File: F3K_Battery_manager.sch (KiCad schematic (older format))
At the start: 12 parts, among them J5 Debug, J6 Serial, J7 Receiver, Q1 CSD13385F5, Q2 CSD13385F5, U1 DRV5032

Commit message: added antenna into schematic
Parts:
- added AE?: Antenna_Loop, symbol Antenna_Loop
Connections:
- no-connect marks 0 -> 2
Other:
- note added: "Antenna - only for Kicost\n"
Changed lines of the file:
@@
 Wire Wire Line
 	2000 4600 2100 4600
+$Comp
+L Antenna_Loop AE?
+U 1 1 5AB2F1C7
+P 1150 4150
+F 0 "AE?" H 1200 4400 50  0000 C CNN
+F 1 "Antenna_Loop" H 1200 4350 50  0000 C CNN
+F 2 "" H 1150 4150 50  0001 C CNN
+F 3 "https://www.vishay.com/docs/34338/iwas3827.pdf" H 1150 4150 50  0001 C CNN
+F 4 "IWAS3827ECEB100J50" H 1150 4150 60  0001 C CNN "MPN"
+	1    1150 4150
+	0    -1   -1   0
+$EndComp
+NoConn ~ 1350 4050
+NoConn ~ 1350 4150
+Text Notes 650  3800 0    60   ~ 0
+Antenna - only for Kicost\n
 $EndSCHEMATC

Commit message: Updated MCU pinout
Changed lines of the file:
@@
 F14 "Voltage_control" O R 6600 4000 60
 F15 "Enable_boost" O R 6600 4200 60
+F16 "Charge_control" O L 4850 4550 60
 $EndSheet
 $Comp
@@
 Text Notes 650  3800 0    60   ~ 0
 Antenna - only for Kicost\n
+Wire Wire Line
+	4250 4550 4850 4550
 $EndSCHEMATC

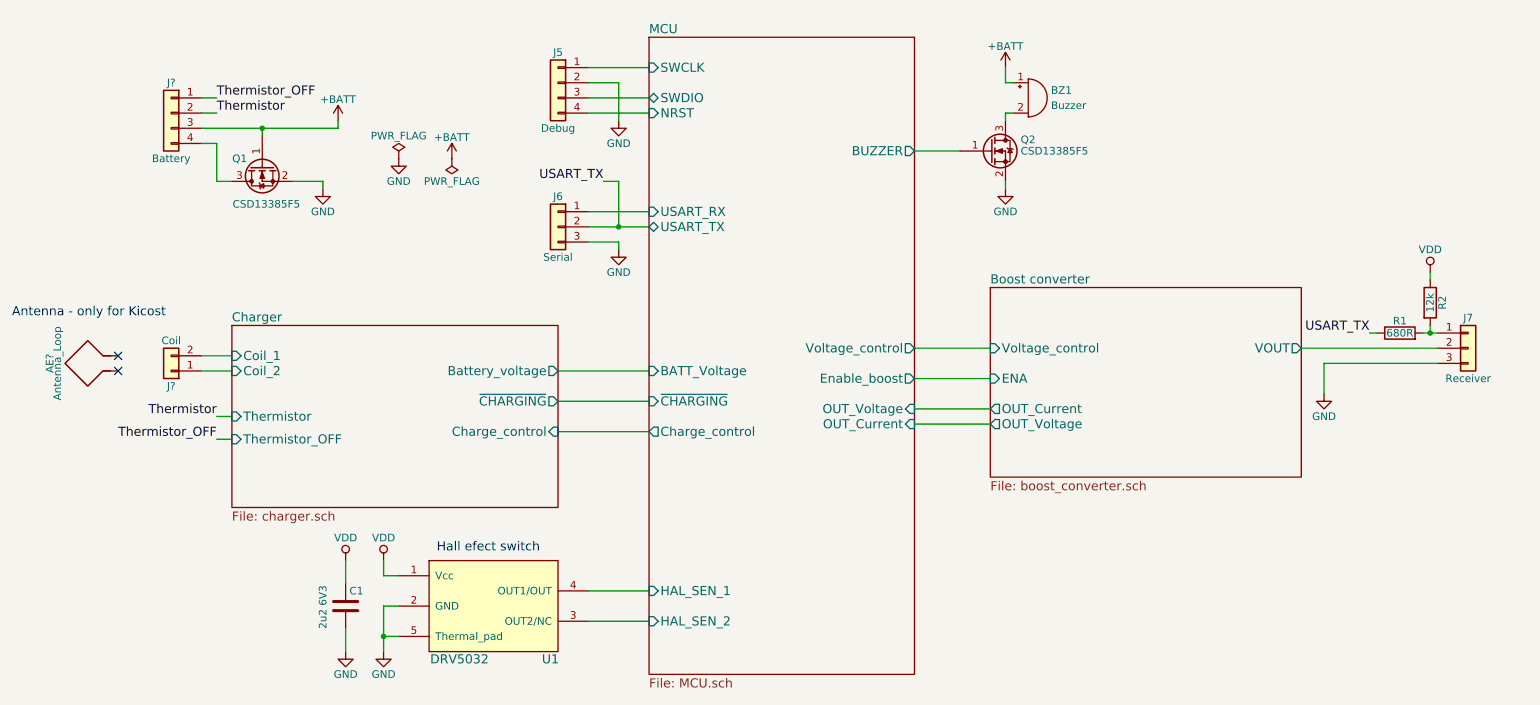
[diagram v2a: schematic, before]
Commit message: Simplified schematic, changed pinout
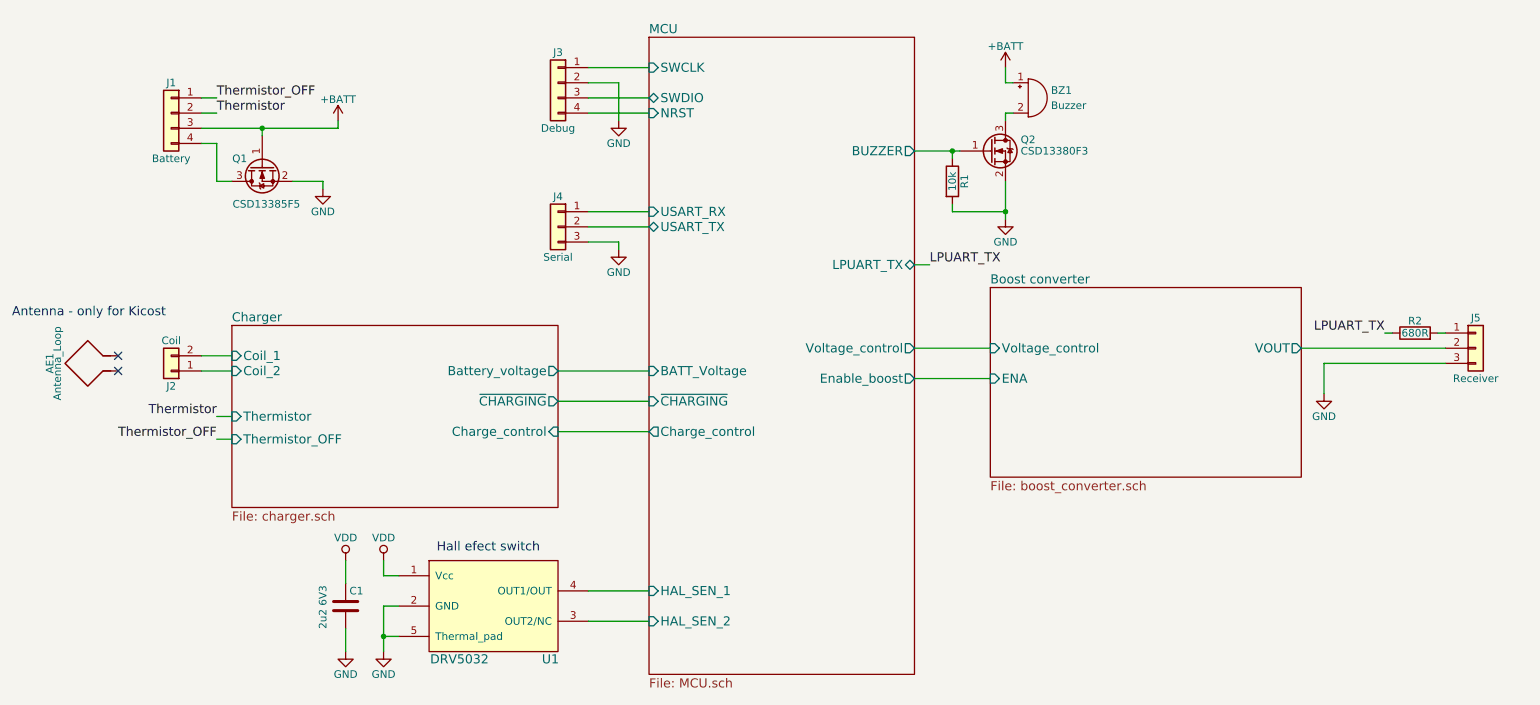
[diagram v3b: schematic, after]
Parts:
- removed Q2: CSD13385F5, symbol CSD13385F5
- removed R2: 12k, symbol R
- added Q2: CSD13380F3, symbol CSD13380F3
- added R1: 10k, Resistors_SMD:R_0402, symbol R
- R2: renamed from R1; footprint (none) -> Resistors_SMD:R_0402
- gave numbers to parts that had none: 3
- renumbered J5 to J3, J6 to J4, J7 to J5
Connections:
- net GND: now also Q2.2 (S), R1.2
- net MCU/BUZZER: now also Q2.1 (G), R1.1
- net at BZ1.2 (+): now also Q2.3 (D)
- net USART_TX renamed LPUART_TX
- net LPUART_TX: no longer J4.2 (Pin_2)
- new net MCU/USART_TX: J4.2 (Pin_2)
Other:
- moved on the sheet: J5, R2
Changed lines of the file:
@@
 F7 "HAL_SEN_2" I L 4850 5800 60
 F8 "BUZZER" O R 6600 2700 60
-F9 "OUT_Voltage" I R 6600 4400 60
-F10 "OUT_Current" I R 6600 4500 60
-F11 "BATT_Voltage" I L 4850 4150 60
-F12 "USART_TX" B L 4850 3200 60
-F13 "~CHARGING" I L 4850 4350 60
-F14 "Voltage_control" O R 6600 4000 60
-F15 "Enable_boost" O R 6600 4200 60
-F16 "Charge_control" O L 4850 4550 60
+F9 "BATT_Voltage" I L 4850 4150 60
+F10 "USART_TX" B L 4850 3200 60
+F11 "~CHARGING" I L 4850 4350 60
+F12 "Voltage_control" O R 6600 4000 60
+F13 "Enable_boost" O R 6600 4200 60
+F14 "Charge_control" O L 4850 4550 60
+F15 "LPUART_TX" B R 6600 3450 60
 $EndSheet
 $Comp
-L Conn_01x04 J5
+L Conn_01x04 J3
 U 1 1 5AA070CB
 P 4250 2250
-F 0 "J5" H 4250 2450 50  0000 C CNN
+F 0 "J3" H 4250 2450 50  0000 C CNN
 F 1 "Debug" H 4250 1950 50  0000 C CNN
 F 2 "" H 4250 2250 50  0001 C CNN
@@
 $EndComp
 $Comp
-L GND #PWR9
+L GND #PWR01
 U 1 1 5AA0735F
 P 4650 2500
-F 0 "#PWR9" H 4650 2250 50  0001 C CNN
+F 0 "#PWR01" H 4650 2250 50  0001 C CNN
 F 1 "GND" H 4650 2350 50  0000 C CNN
 F 2 "" H 4650 2500 50  0001 C CNN
@@
 $EndComp
 $Comp
-L GND #PWR10
+L GND #PWR02
 U 1 1 5AA07C91
 P 4650 3350
-F 0 "#PWR10" H 4650 3100 50  0001 C CNN
+F 0 "#PWR02" H 4650 3100 50  0001 C CNN
 F 1 "GND" H 4650 3200 50  0000 C CNN
 F 2 "" H 4650 3350 50  0001 C CNN
@@
 	4650 3300 4650 3350
 $Comp
-L GND #PWR6
+L GND #PWR03
 U 1 1 5AA09559
 P 3100 6000
-F 0 "#PWR6" H 3100 5750 50  0001 C CNN
+F 0 "#PWR03" H 3100 5750 50  0001 C CNN
 F 1 "GND" H 3100 5850 50  0000 C CNN
 F 2 "" H 3100 6000 50  0001 C CNN
@@
 Connection ~ 3100 5900
 $Comp
-L VDD #PWR5
+L VDD #PWR04
 U 1 1 5AA0982A
 P 3100 5400
-F 0 "#PWR5" H 3100 5250 50  0001 C CNN
+F 0 "#PWR04" H 3100 5250 50  0001 C CNN
 F 1 "VDD" H 3100 5550 50  0000 C CNN
 F 2 "" H 3100 5400 50  0001 C CNN
@@
 	3100 5500 3200 5500
 $Comp
-L VDD #PWR3
+L VDD #PWR05
 U 1 1 5AA09936
 P 2850 5400
-F 0 "#PWR3" H 2850 5250 50  0001 C CNN
+F 0 "#PWR05" H 2850 5250 50  0001 C CNN
 F 1 "VDD" H 2850 5550 50  0000 C CNN
 F 2 "" H 2850 5400 50  0001 C CNN
@@
 $EndComp
 $Comp
-L GND #PWR4
+L GND #PWR06
 U 1 1 5AA0996B
 P 2850 6000
-F 0 "#PWR4" H 2850 5750 50  0001 C CNN
+F 0 "#PWR06" H 2850 5750 50  0001 C CNN
 F 1 "GND" H 2850 5850 50  0000 C CNN
 F 2 "" H 2850 6000 50  0001 C CNN
@@
 Wire Wire Line
 	4450 5800 4850 5800
-$Comp
-L PWR_FLAG #FLG1
-U 1 1 5AA0B07D
-P 3200 2750
-F 0 "#FLG1" H 3200 2825 50  0001 C CNN
-F 1 "PWR_FLAG" H 3200 2900 50  0000 C CNN
-F 2 "" H 3200 2750 50  0001 C CNN
-F 3 "" H 3200 2750 50  0001 C CNN
-	1    3200 2750
-	1    0    0    -1
-$EndComp
-$Comp
-L GND #PWR7
-U 1 1 5AA0B18B
-P 3200 2750
-F 0 "#PWR7" H 3200 2500 50  0001 C CNN
-F 1 "GND" H 3200 2600 50  0000 C CNN
-F 2 "" H 3200 2750 50  0001 C CNN
-F 3 "" H 3200 2750 50  0001 C CNN
-	1    3200 2750
-	1    0    0    -1
-$EndComp
-$Comp
-L PWR_FLAG #FLG2
-U 1 1 5AA0B25E
-P 3550 2750
-F 0 "#FLG2" H 3550 2825 50  0001 C CNN
-F 1 "PWR_FLAG" H 3550 2900 50  0000 C CNN
-F 2 "" H 3550 2750 50  0001 C CNN
-F 3 "" H 3550 2750 50  0001 C CNN
-	1    3550 2750
-	-1   0    0    1
-$EndComp
-$Comp
-L +BATT #PWR8
-U 1 1 5AA0B29D
-P 3550 2750
-F 0 "#PWR8" H 3550 2600 50  0001 C CNN
-F 1 "+BATT" H 3550 2890 50  0000 C CNN
-F 2 "" H 3550 2750 50  0001 C CNN
-F 3 "" H 3550 2750 50  0001 C CNN
-	1    3550 2750
-	1    0    0    -1
-$EndComp
 $Comp
 L Buzzer BZ1
@@
 	7200 2450 7200 2500
 $Comp
-L GND #PWR12
+L GND #PWR07
 U 1 1 5AA112B0
-P 7200 2950
-F 0 "#PWR12" H 7200 2700 50  0001 C CNN
-F 1 "GND" H 7200 2800 50  0000 C CNN
-F 2 "" H 7200 2950 50  0001 C CNN
-F 3 "" H 7200 2950 50  0001 C CNN
-	1    7200 2950
-	1    0    0    -1
-$EndComp
-Wire Wire Line
-	7200 2900 7200 2950
+P 7200 3150
+F 0 "#PWR07" H 7200 2900 50  0001 C CNN
+F 1 "GND" H 7200 3000 50  0000 C CNN
+F 2 "" H 7200 3150 50  0001 C CNN
+F 3 "" H 7200 3150 50  0001 C CNN
+	1    7200 3150
+	1    0    0    -1
+$EndComp
+Wire Wire Line
+	7200 2900 7200 3150
 Wire Wire Line
 	6600 2700 6900 2700
 $Comp
-L +BATT #PWR11
+L +BATT #PWR08
 U 1 1 5AA3F1DA
 P 7200 2150
-F 0 "#PWR11" H 7200 2000 50  0001 C CNN
+F 0 "#PWR08" H 7200 2000 50  0001 C CNN
 F 1 "+BATT" H 7200 2290 50  0000 C CNN
 F 2 "" H 7200 2150 50  0001 C CNN
@@
 F2 "VOUT" O R 9150 4000 60
 F3 "ENA" I L 7100 4200 60
-F4 "OUT_Current" O L 7100 4400 60
-F5 "OUT_Voltage" O L 7100 4500 60
-F6 "Voltage_control" I L 7100 4000 60
+F4 "Voltage_control" I L 7100 4000 60
 $EndSheet
 Wire Wire Line
-	7100 4400 6600 4400
-Wire Wire Line
-	6600 4500 7100 4500
-Wire Wire Line
 	6600 4200 7100 4200
 Wire Wire Line
 	6600 4000 7100 4000
 $Comp
-L Conn_01x03 J7
+L Conn_01x03 J5
 U 1 1 5AA45C5D
-P 10250 4000
-F 0 "J7" H 10250 4200 50  0000 C CNN
-F 1 "Receiver" H 10250 3800 50  0000 C CNN
-F 2 "" H 10250 4000 50  0001 C CNN
-F 3 "" H 10250 4000 50  0001 C CNN
-	1    10250 4000
-	1    0    0    -1
-$EndComp
-Wire Wire Line
-	9150 4000 10050 4000
-$Comp
-L GND #PWR13
+P 10300 4000
+F 0 "J5" H 10300 4200 50  0000 C CNN
+F 1 "Receiver" H 10300 3800 50  0000 C CNN
+F 2 "" H 10300 4000 50  0001 C CNN
+F 3 "" H 10300 4000 50  0001 C CNN
+	1    10300 4000
+	1    0    0    -1
+$EndComp
+Wire Wire Line
+	9150 4000 10100 4000
+$Comp
+L GND #PWR09
 U 1 1 5AA460B2
 P 9300 4300
-F 0 "#PWR13" H 9300 4050 50  0001 C CNN
+F 0 "#PWR09" H 9300 4050 50  0001 C CNN
 F 1 "GND" H 9300 4150 50  0000 C CNN
 F 2 "" H 9300 4300 50  0001 C CNN
@@
 $EndComp
 Wire Wire Line
-	10050 4100 9300 4100
+	10100 4100 9300 4100
 Wire Wire Line
 	9300 4100 9300 4300
 $Comp
-L Conn_01x03 J6
+L Conn_01x03 J4
 U 1 1 5AA46769
 P 4250 3200
-F 0 "J6" H 4250 3400 50  0000 C CNN
+F 0 "J4" H 4250 3400 50  0000 C CNN
 F 1 "Serial" H 4250 3000 50  0000 C CNN
 F 2 "" H 4250 3200 50  0001 C CNN
@@
 Hall efect switch\n
 $Comp
-L R R1
+L R R2
 U 1 1 5AA59CAF
-P 9800 3900
-F 0 "R1" V 9880 3900 50  0000 C CNN
-F 1 "680R" V 9800 3900 50  0000 C CNN
-F 2 "" V 9730 3900 50  0001 C CNN
-F 3 "" H 9800 3900 50  0001 C CNN
-	1    9800 3900
+P 9900 3900
+F 0 "R2" V 9980 3900 50  0000 C CNN
+F 1 "680R" V 9900 3900 50  0000 C CNN
+F 2 "Resistors_SMD:R_0402" V 9830 3900 50  0001 C CNN
+F 3 "" H 9900 3900 50  0001 C CNN
+	1    9900 3900
 	0    -1   -1   0
 $EndComp
 Wire Wire Line
-	9950 3900 10050 3900
-Text Label 4550 2900 2    60   ~ 0
-USART_TX
-Wire Wire Line
-	4550 2900 4650 2900
-Wire Wire Line
-	4650 2900 4650 3200
-Connection ~ 4650 3200
-Text Label 9600 3900 2    60   ~ 0
-USART_TX
-Wire Wire Line
-	9600 3900 9650 3900
-$Comp
-L R R2
-U 1 1 5AA65085
-P 10000 3700
-F 0 "R2" V 10080 3700 50  0000 C CNN
-F 1 "12k" V 10000 3700 50  0000 C CNN
-F 2 "" V 9930 3700 50  0001 C CNN
-F 3 "" H 10000 3700 50  0001 C CNN
-	1    10000 3700
-	1    0    0    -1
-$EndComp
-Wire Wire Line
-	10000 3850 10000 3900
-Connection ~ 10000 3900
-$Comp
-L VDD #PWR14
-U 1 1 5AA65702
-P 10000 3500
-F 0 "#PWR14" H 10000 3350 50  0001 C CNN
-F 1 "VDD" H 10000 3650 50  0000 C CNN
-F 2 "" H 10000 3500 50  0001 C CNN
-F 3 "" H 10000 3500 50  0001 C CNN
-	1    10000 3500
-	1    0    0    -1
-$EndComp
-Wire Wire Line
-	10000 3500 10000 3550
+	10050 3900 10100 3900
+Text Label 6700 3450 0    60   ~ 0
+LPUART_TX
+Wire Wire Line
+	9700 3900 9750 3900
 Wire Wire Line
 	4250 4150 4850 4150
-$Comp
-L CSD13385F5 Q2
-U 1 1 5AA727C4
-P 7100 2700
-F 0 "Q2" H 7300 2775 50  0000 L CNN
-F 1 "CSD13385F5" H 7300 2700 50  0000 L CNN
-F 2 "" H 7300 2625 50  0001 L CIN
-F 3 "http://www.ti.com/lit/ds/symlink/csd13385f5.pdf" H 6400 2400 50  0001 L CNN
-F 4 "CSD13385F5" H 7200 3000 60  0001 C CNN "MPN"
-	1    7100 2700
-	1    0    0    -1
-$EndComp
 $Comp
 L CSD13385F5 Q1
@@
 	2300 2550 2300 2550
 $Comp
-L +BATT #PWR1
+L +BATT #PWR010
 U 1 1 5AA74E47
 P 2800 2500
-F 0 "#PWR1" H 2800 2350 50  0001 C CNN
+F 0 "#PWR010" H 2800 2350 50  0001 C CNN
 F 1 "+BATT" H 2800 2640 50  0000 C CNN
 F 2 "" H 2800 2500 50  0001 C CNN
@@
 Connection ~ 2300 2550
 $Comp
-L GND #PWR2
+L GND #PWR011
 U 1 1 5AA7526D
 P 2700 2950
-F 0 "#PWR2" H 2700 2700 50  0001 C CNN
+F 0 "#PWR011" H 2700 2700 50  0001 C CNN
 F 1 "GND" H 2700 2800 50  0000 C CNN
 F 2 "" H 2700 2950 50  0001 C CNN
@@
 	2700 2900 2700 2950
 $Comp
-L Conn_01x04 J?
+L Conn_01x04 J1
 U 1 1 5AB08D80
 P 1700 2450
-F 0 "J?" H 1700 2650 50  0000 C CNN
+F 0 "J1" H 1700 2650 50  0000 C CNN
 F 1 "Battery" H 1700 2150 50  0000 C CNN
 F 2 "" H 1700 2450 50  0001 C CNN
@@
 $EndSheet
 $Comp
-L Conn_01x02 J?
+L Conn_01x02 J2
 U 1 1 5AB11894
 P 1700 4150
-F 0 "J?" H 1700 4250 50  0000 C CNN
+F 0 "J2" H 1700 4250 50  0000 C CNN
 F 1 "Coil" H 1700 3950 50  0000 C CNN
 F 2 "" H 1700 4150 50  0001 C CNN
@@
 	2000 4600 2100 4600
 $Comp
-L Antenna_Loop AE?
+L Antenna_Loop AE1
 U 1 1 5AB2F1C7
 P 1150 4150
-F 0 "AE?" H 1200 4400 50  0000 C CNN
+F 0 "AE1" H 1200 4400 50  0000 C CNN
 F 1 "Antenna_Loop" H 1200 4350 50  0000 C CNN
 F 2 "" H 1150 4150 50  0001 C CNN
@@
 Wire Wire Line
 	4250 4550 4850 4550
+$Comp
+L CSD13380F3 Q2
+U 1 1 5AB5A73F
+P 7100 2700
+F 0 "Q2" H 7300 2775 50  0000 L CNN
+F 1 "CSD13380F3" H 7300 2700 50  0000 L CNN
+F 2 "" H 7300 2625 50  0001 L CIN
+F 3 "http://www.ti.com/product/CSD13380F3" H 6400 2400 50  0001 L CNN
+	1    7100 2700
+	1    0    0    -1
+$EndComp
+$Comp
+L R R1
+U 1 1 5AB6270F
+P 6850 2900
+F 0 "R1" V 6930 2900 50  0000 C CNN
+F 1 "10k" V 6850 2900 50  0000 C CNN
+F 2 "Resistors_SMD:R_0402" V 6780 2900 50  0001 C CNN
+F 3 "" H 6850 2900 50  0001 C CNN
+	1    6850 2900
+	1    0    0    -1
+$EndComp
+Wire Wire Line
+	6850 2750 6850 2700
+Connection ~ 6850 2700
+Wire Wire Line
+	6850 3050 6850 3100
+Wire Wire Line
+	6850 3100 7200 3100
+Connection ~ 7200 3100
+Wire Wire Line
+	6700 3450 6600 3450
+Text Label 9700 3900 2    60   ~ 0
+LPUART_TX
 $EndSCHEMATC

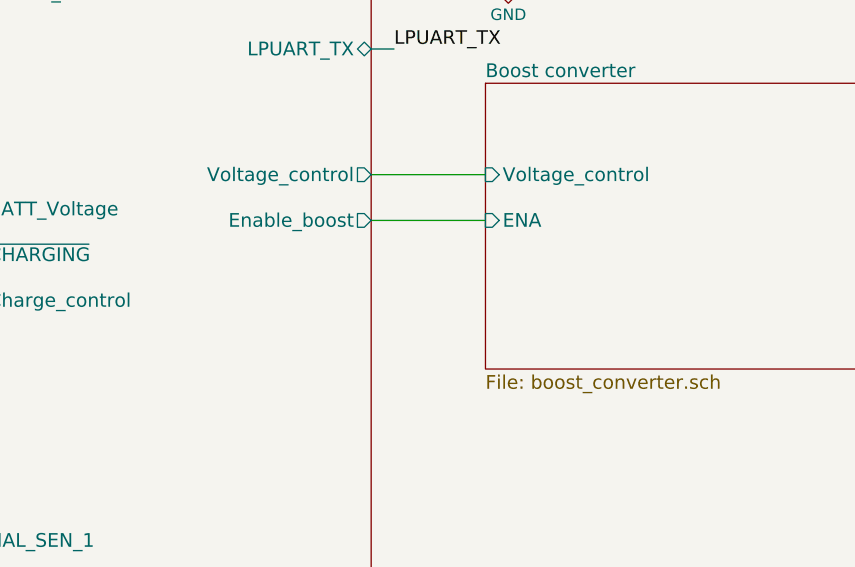
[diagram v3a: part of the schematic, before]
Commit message: Changed pinout, added voltage and current reading
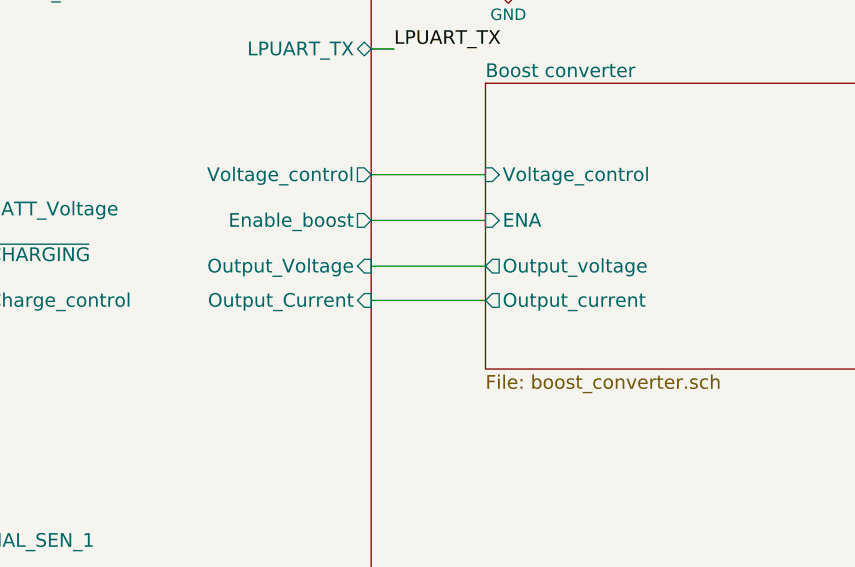
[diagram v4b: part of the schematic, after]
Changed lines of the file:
@@
 F14 "Charge_control" O L 4850 4550 60
 F15 "LPUART_TX" B R 6600 3450 60
+F16 "Output_Voltage" I R 6600 4400 60
+F17 "Output_Current" I R 6600 4550 60
 $EndSheet
 $Comp
@@
 $EndComp
 $Comp
-L GND #PWR01
+L GND #PWR7
 U 1 1 5AA0735F
 P 4650 2500
-F 0 "#PWR01" H 4650 2250 50  0001 C CNN
+F 0 "#PWR7" H 4650 2250 50  0001 C CNN
 F 1 "GND" H 4650 2350 50  0000 C CNN
 F 2 "" H 4650 2500 50  0001 C CNN
@@
 $EndComp
 $Comp
-L GND #PWR02
+L GND #PWR8
 U 1 1 5AA07C91
 P 4650 3350
-F 0 "#PWR02" H 4650 3100 50  0001 C CNN
+F 0 "#PWR8" H 4650 3100 50  0001 C CNN
 F 1 "GND" H 4650 3200 50  0000 C CNN
 F 2 "" H 4650 3350 50  0001 C CNN
@@
 	4650 3300 4650 3350
 $Comp
-L GND #PWR03
+L GND #PWR6
 U 1 1 5AA09559
 P 3100 6000
-F 0 "#PWR03" H 3100 5750 50  0001 C CNN
+F 0 "#PWR6" H 3100 5750 50  0001 C CNN
 F 1 "GND" H 3100 5850 50  0000 C CNN
 F 2 "" H 3100 6000 50  0001 C CNN
@@
 Connection ~ 3100 5900
 $Comp
-L VDD #PWR04
+L VDD #PWR5
 U 1 1 5AA0982A
 P 3100 5400
-F 0 "#PWR04" H 3100 5250 50  0001 C CNN
+F 0 "#PWR5" H 3100 5250 50  0001 C CNN
 F 1 "VDD" H 3100 5550 50  0000 C CNN
 F 2 "" H 3100 5400 50  0001 C CNN
@@
 	3100 5500 3200 5500
 $Comp
-L VDD #PWR05
+L VDD #PWR3
 U 1 1 5AA09936
 P 2850 5400
-F 0 "#PWR05" H 2850 5250 50  0001 C CNN
+F 0 "#PWR3" H 2850 5250 50  0001 C CNN
 F 1 "VDD" H 2850 5550 50  0000 C CNN
 F 2 "" H 2850 5400 50  0001 C CNN
@@
 $EndComp
 $Comp
-L GND #PWR06
+L GND #PWR4
 U 1 1 5AA0996B
 P 2850 6000
-F 0 "#PWR06" H 2850 5750 50  0001 C CNN
+F 0 "#PWR4" H 2850 5750 50  0001 C CNN
 F 1 "GND" H 2850 5850 50  0000 C CNN
 F 2 "" H 2850 6000 50  0001 C CNN
@@
 	7200 2450 7200 2500
 $Comp
-L GND #PWR07
+L GND #PWR10
 U 1 1 5AA112B0
 P 7200 3150
-F 0 "#PWR07" H 7200 2900 50  0001 C CNN
+F 0 "#PWR10" H 7200 2900 50  0001 C CNN
 F 1 "GND" H 7200 3000 50  0000 C CNN
 F 2 "" H 7200 3150 50  0001 C CNN
@@
 	6600 2700 6900 2700
 $Comp
-L +BATT #PWR08
+L +BATT #PWR9
 U 1 1 5AA3F1DA
 P 7200 2150
-F 0 "#PWR08" H 7200 2000 50  0001 C CNN
+F 0 "#PWR9" H 7200 2000 50  0001 C CNN
 F 1 "+BATT" H 7200 2290 50  0000 C CNN
 F 2 "" H 7200 2150 50  0001 C CNN
@@
 F3 "ENA" I L 7100 4200 60
 F4 "Voltage_control" I L 7100 4000 60
+F5 "Output_voltage" O L 7100 4400 60
+F6 "Output_current" O L 7100 4550 60
 $EndSheet
 Wire Wire Line
@@
 	9150 4000 10100 4000
 $Comp
-L GND #PWR09
+L GND #PWR11
 U 1 1 5AA460B2
 P 9300 4300
-F 0 "#PWR09" H 9300 4050 50  0001 C CNN
+F 0 "#PWR11" H 9300 4050 50  0001 C CNN
 F 1 "GND" H 9300 4150 50  0000 C CNN
 F 2 "" H 9300 4300 50  0001 C CNN
@@
 	2300 2550 2300 2550
 $Comp
-L +BATT #PWR010
+L +BATT #PWR2
 U 1 1 5AA74E47
 P 2800 2500
-F 0 "#PWR010" H 2800 2350 50  0001 C CNN
+F 0 "#PWR2" H 2800 2350 50  0001 C CNN
 F 1 "+BATT" H 2800 2640 50  0000 C CNN
 F 2 "" H 2800 2500 50  0001 C CNN
@@
 Connection ~ 2300 2550
 $Comp
-L GND #PWR011
+L GND #PWR1
 U 1 1 5AA7526D
 P 2700 2950
-F 0 "#PWR011" H 2700 2700 50  0001 C CNN
+F 0 "#PWR1" H 2700 2700 50  0001 C CNN
 F 1 "GND" H 2700 2800 50  0000 C CNN
 F 2 "" H 2700 2950 50  0001 C CNN
@@
 Text Label 9700 3900 2    60   ~ 0
 LPUART_TX
+Wire Wire Line
+	6600 4400 7100 4400
+Wire Wire Line
+	6600 4550 7100 4550
 $EndSCHEMATC
